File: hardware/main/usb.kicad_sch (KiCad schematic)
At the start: 0 parts

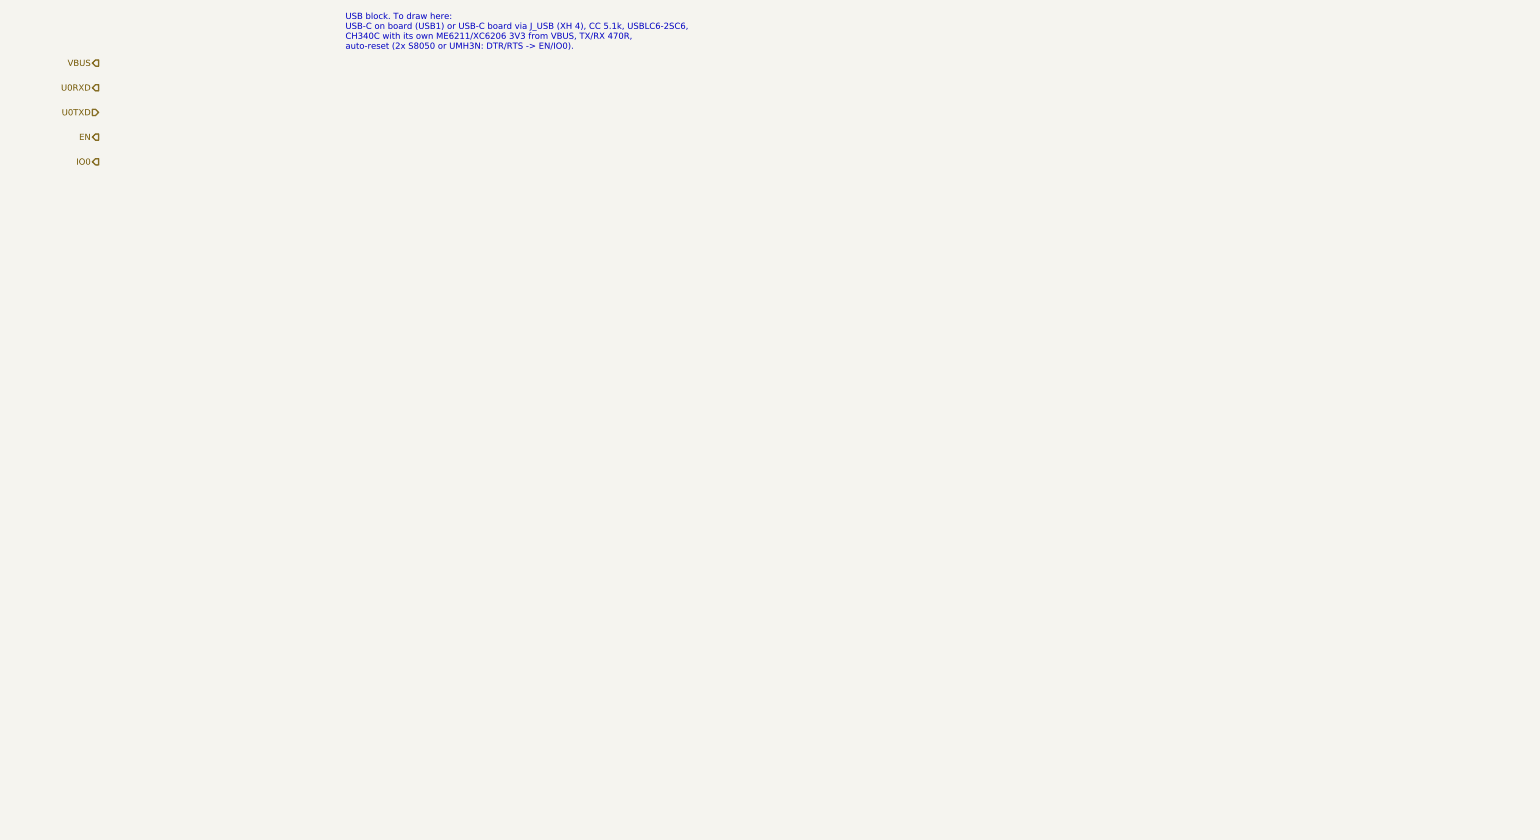
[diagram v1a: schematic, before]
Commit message: hardware: USB, Audio and Connectors sheets; main board ERC clean
Co-Authored-By: Claude Opus 5.5 <noreply@anthropic.com>
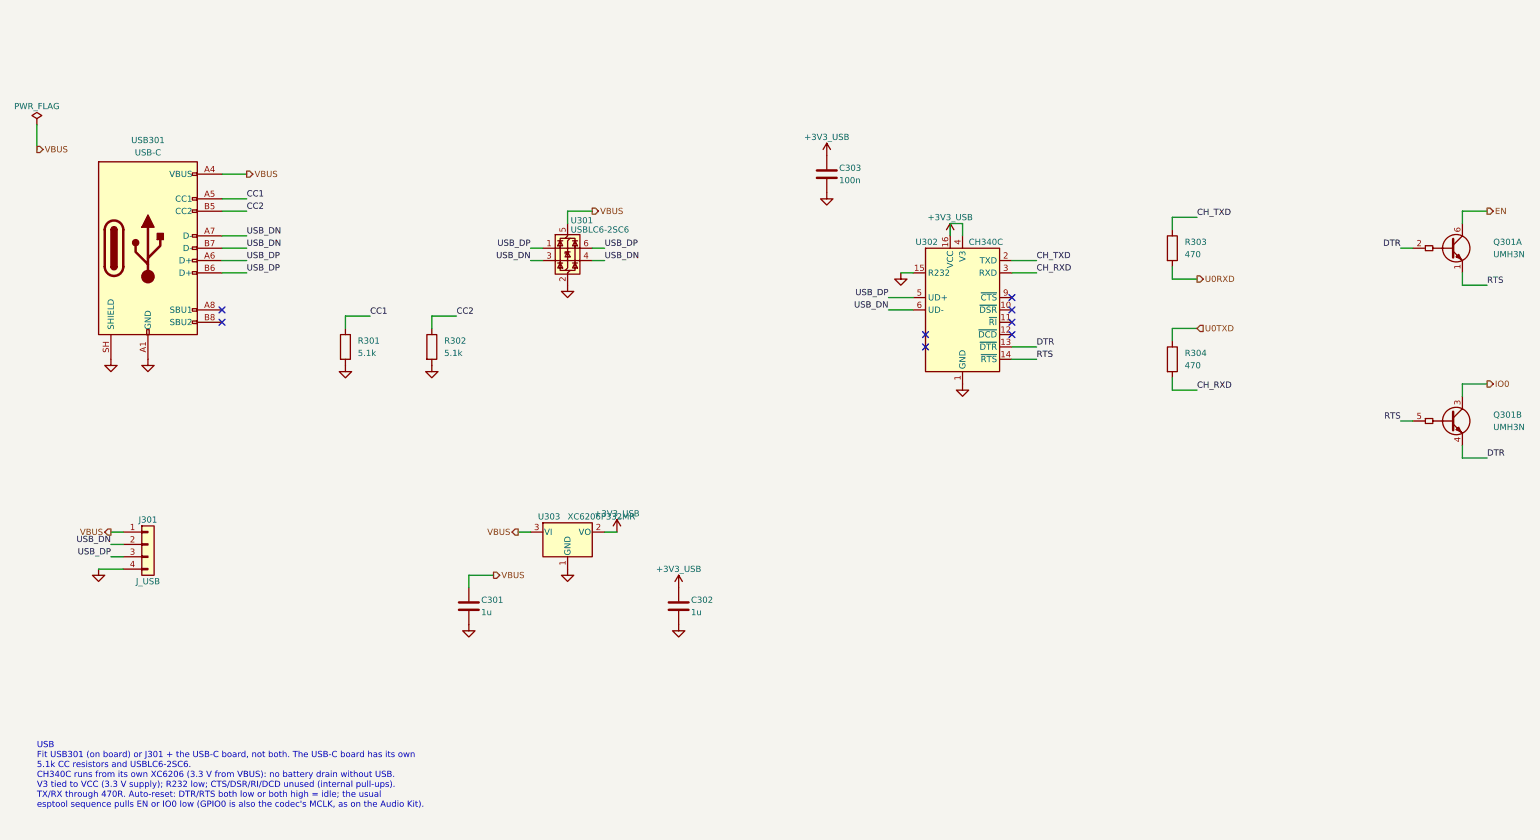
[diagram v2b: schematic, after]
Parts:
- added C301, C302: 1u, Capacitor_SMD:C_0805_2012Metric, symbol Device:C
- added C303: 100n, Capacitor_SMD:C_0805_2012Metric, symbol Device:C
- added J301: J_USB, Connector_JST:JST_XH_B4B-XH-A_1x04_P2.50mm_Vertical, symbol Connector_Generic:Conn_01x04
- added Q301: UMH3N, Package_TO_SOT_SMD:SOT-363_SC-70-6, symbol Transistor_BJT:UMH3N
- added R301, R302: 5.1k, Resistor_SMD:R_0805_2012Metric, symbol Device:R
- added R303, R304: 470, Resistor_SMD:R_0805_2012Metric, symbol Device:R
- added U301: USBLC6-2SC6, Package_TO_SOT_SMD:SOT-23-6, symbol Power_Protection:USBLC6-2SC6
- added U302: CH340C, Package_SO:SOIC-16_3.9x9.9mm_P1.27mm, symbol sendspin-speaker:CH340C
- added U303: XC6206P332MR, Package_TO_SOT_SMD:SOT-23-3, symbol Regulator_Linear:XC6206PxxxMR
- added USB301: USB-C, Connector_USB:USB_C_Receptacle_HRO_TYPE-C-31-M-12, symbol Connector:USB_C_Receptacle_USB2.0_16P
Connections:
- net EN: now also Q301.6 (C1)
- net IO0: now also Q301.3 (C2)
- net U0RXD: now also R303.2
- net U0TXD: now also R304.1
- net VBUS: now also C301.1, J301.1 (Pin_1), U301.5 (VBUS), U303.3 (VI), USB301.A4 (VBUS), USB301.A9 (VBUS), USB301.B4 (VBUS), USB301.B9 (VBUS)
- new net +3V3_USB: C302.1, C303.1, U302.16 (VCC), U302.4 (V3), U303.2 (VO)
- new net CC1: R301.1, USB301.A5 (CC1)
- new net CC2: R302.1, USB301.B5 (CC2)
- new net CH_RXD: R304.2, U302.3 (RXD)
- new net CH_TXD: R303.1, U302.2 (TXD)
- new net DTR: Q301.2 (B1), Q301.4 (E2), U302.13 (~{DTR})
- new net GND: C301.2, C302.2, C303.2, J301.4 (Pin_4), R301.2, R302.2, U301.2 (GND), U302.1 (GND), U302.15 (R232), U303.1 (GND), USB301.A1 (GND), USB301.A12 (GND), USB301.B1 (GND), USB301.B12 (GND), USB301.SH (SHIELD)
- new net RTS: Q301.1 (E1), Q301.5 (B2), U302.14 (~{RTS})
- new net USB_DN: J301.2 (Pin_2), U301.3 (I/O2), U301.4 (I/O2), U302.6 (UD-), USB301.A7 (D-), USB301.B7 (D-)
- new net USB_DP: J301.3 (Pin_3), U301.1 (I/O1), U301.6 (I/O1), U302.5 (UD+), USB301.A6 (D+), USB301.B6 (D+)
- no-connect marks 0 -> 8
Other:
- note added: "USB Fit USB301 (on board) or J301 + the USB-C board, not both. The USB-C board has its own 5.1k CC resistors and USBLC6-2SC6. CH340C runs from its own XC6206 (3.3 V from VBUS): no battery drain without USB. V3 tied to VCC (3.3 V supply); R232 low; CTS/DSR/RI/DCD unused (internal pull-ups). TX/RX through 470R. Auto-reset: DTR/RTS both low or both high = idle; the usual esptool sequence pulls EN or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"
- note removed: "USB block. To draw here: USB-C on board (USB1) or USB-C board via J_USB (XH 4), CC 5.1k, USBLC6-2SC6, CH340C with its own ME6211/XC6206 3V3 from VBUS, TX/RX 470R, auto-reset (2x S8050 or UMH3N: DTR/RTS -> EN/IO0)."

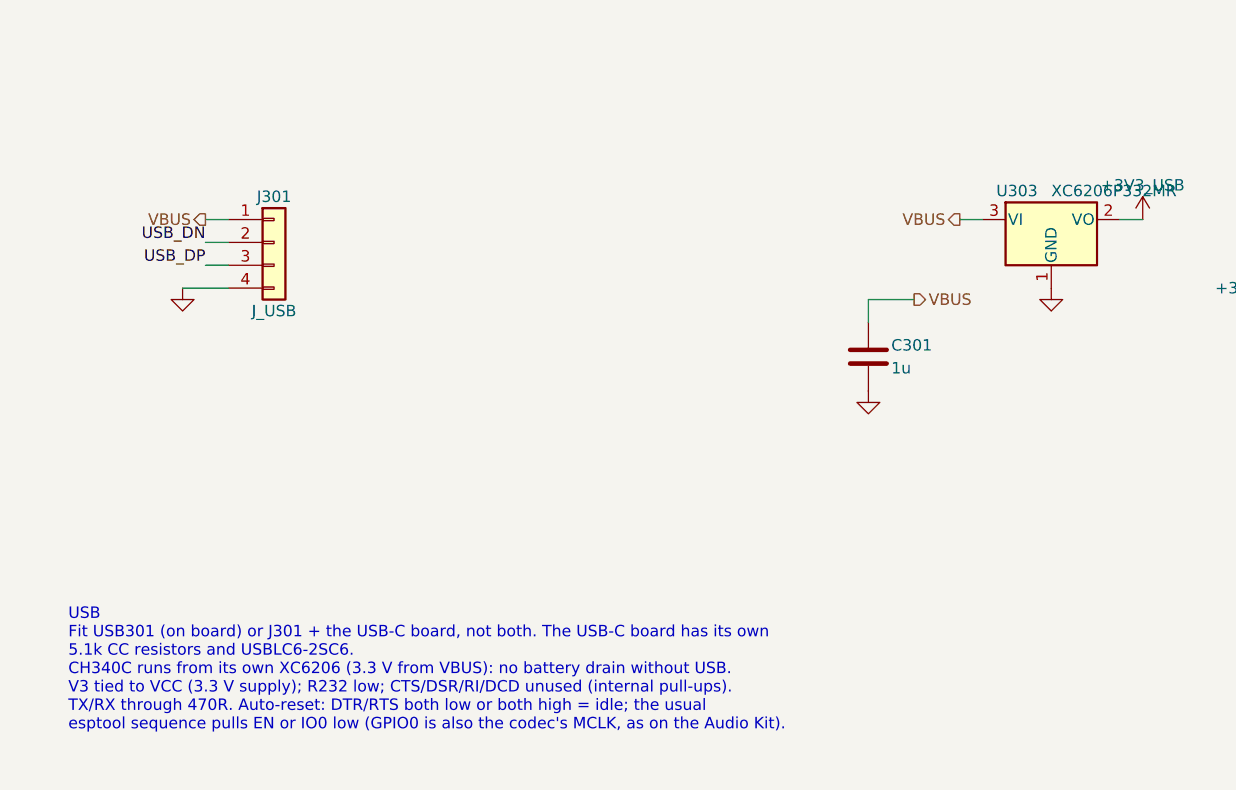
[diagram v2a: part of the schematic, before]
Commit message: hardware: bare USB-C board and front panel (schematics)
J_USB carries CC1/CC2 (XH 6); CC resistors and ESD stay on the main
board. Front panel has only buttons and headers; its LED pin comes
through R501. Boards not yet updated from the schematics.

Co-Authored-By: Claude Opus 5.5 <noreply@anthropic.com>
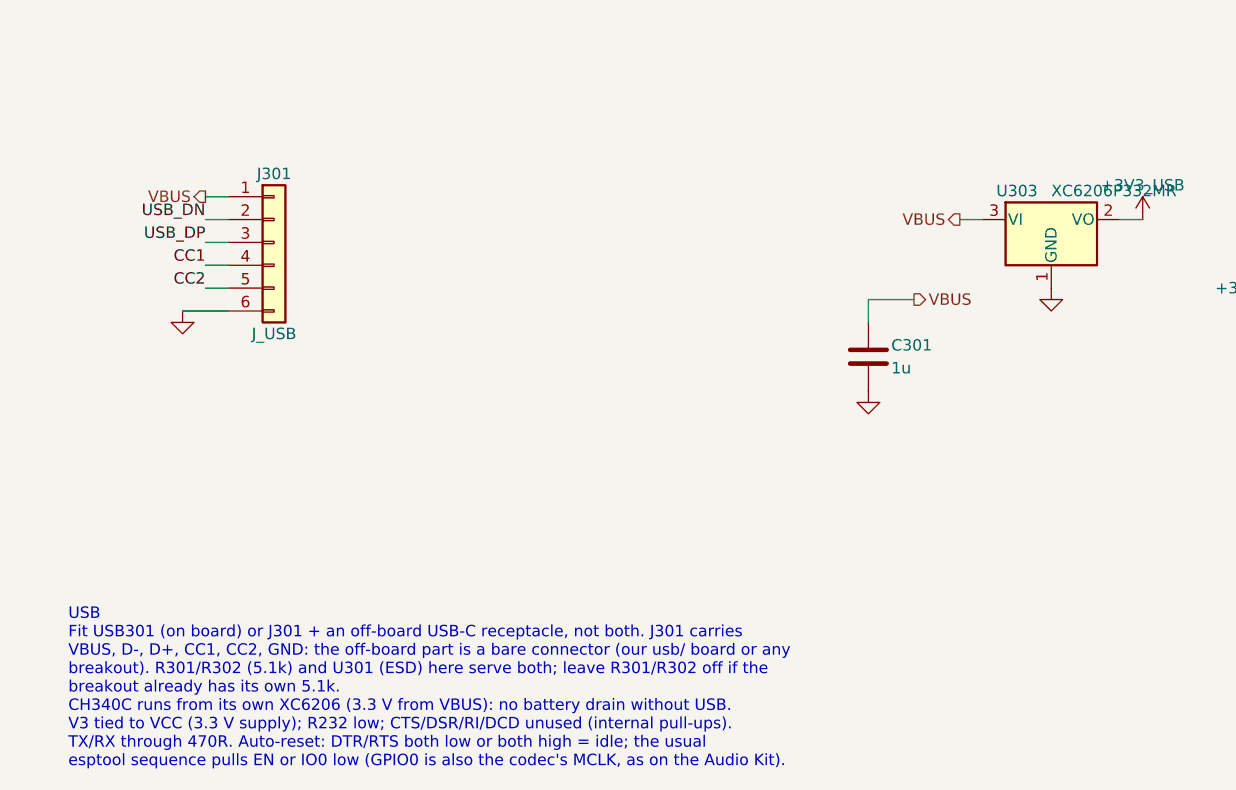
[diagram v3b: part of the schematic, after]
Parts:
- removed J301: J_USB, Connector_JST:JST_XH_B4B-XH-A_1x04_P2.50mm_Vertical, symbol Connector_Generic:Conn_01x04
- added J301: J_USB, Connector_JST:JST_XH_B6B-XH-A_1x06_P2.50mm_Vertical, symbol Connector_Generic:Conn_01x06
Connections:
- net CC1: now also J301.4 (Pin_4)
- net CC2: now also J301.5 (Pin_5)
- net GND: now also J301.6 (Pin_6)
- net USB_DN: now also J301.2 (Pin_2)
- net USB_DP: now also J301.3 (Pin_3)
- net VBUS: now also J301.1 (Pin_1)
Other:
- note added: "USB Fit USB301 (on board) or J301 + an off-board USB-C receptacle, not both. J301 carries VBUS, D-, D+, CC1, CC2, GND: the off-board part is a bare connector (our usb/ board or any breakout). R301/R302 (5.1k) and U301 (ESD) here serve both; leave R301/R302 off if the breakout already has its own 5.1k. CH340C runs from its own XC6206 (3.3 V from VBUS): no battery drain without USB. V3 tied to VCC 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"
- note removed: "USB Fit USB301 (on board) or J301 + the USB-C board, not both. The USB-C board has its own 5.1k CC resistors and USBLC6-2SC6. CH340C runs from its own XC6206 (3.3 V from VBUS): no battery drain without USB. V3 tied to VCC (3.3 V supply); R232 low; CTS/DSR/RI/DCD unused (internal pull-ups). TX/RX through 470R. Auto-reset: DTR/RTS both low or both high = idle; the usual esptool sequence pulls EN or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"

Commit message: hardware: main board routed and labelled, JLC files
- Freerouting (jar, portable Java 25) via scripts/route.py; net classes
  Power 0.8 mm / Supply 0.4 mm so tracks fit the fine-pitch pins.
- Silkscreen pin names and function labels (silk_main.py), references on
  the fab layer, SMD GND pads solid to the pour; board 100 x 58 mm.
- LCSC numbers on all SMD parts (checked on lcsc.com); jlc.py writes the
  Gerber ZIP, BOM and CPL in JLC's formats.

Co-Authored-By: Claude Opus 5.5 <noreply@anthropic.com>
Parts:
- C301, C302: LCSC (none) -> C28323
- C303: LCSC (none) -> C49678
- Q301: LCSC (none) -> C123008
- R301, R302: LCSC (none) -> C27834
- R303, R304: LCSC (none) -> C17710
- U301: LCSC (none) -> C7519
- U302: LCSC (none) -> C84681
- U303: LCSC (none) -> C5446
- USB301: LCSC (none) -> C165948
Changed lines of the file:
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@@
+			)
+		)
+		(property "LCSC" "C84681"
+			(at 0 0 0)
+			(hide yes)
+			(effects
+				(font
+					(size 1.27 1.27)
+				)
 			)
 		)
@@
 			)
 		)
+		(property "LCSC" "C27834"
+			(at 0 0 0)
+			(hide yes)
+			(effects
+				(font
+					(size 1.27 1.27)
+				)
+			)
+		)
 		(property "Description" ""
 			(at 119.38 109.22 0)
@@
 			)
 		)
+		(property "LCSC" "C123008"
+			(at 0 0 0)
+			(hide yes)
+			(effects
+				(font
+					(size 1.27 1.27)
+				)
+			)
+		)
 		(property "Description" ""
 			(at 330.2 88.9 0)
@@
 			)
 		)
+		(property "LCSC" "C5446"
+			(at 0 0 0)
+			(hide yes)
+			(effects
+				(font
+					(size 1.27 1.27)
+				)
+			)
+		)
 		(property "Description" ""
 			(at 147.32 147.32 0)
@@
 			)
 		)
+		(property "LCSC" "C27834"
+			(at 0 0 0)
+			(hide yes)
+			(effects
+				(font
+					(size 1.27 1.27)
+				)
+			)
+		)
 		(property "Description" ""
 			(at 101.6 109.22 0)
@@
 			)
 		)
+		(property "LCSC" "C17710"
+			(at 0 0 0)
+			(hide yes)
+			(effects
+				(font
+					(size 1.27 1.27)
+				)
+			)
+		)
 		(property "Description" ""
 			(at 271.78 88.9 0)
@@
 			)
 		)
+		(property "LCSC" "C28323"
+			(at 0 0 0)
+			(hide yes)
+			(effects
+				(font
+					(size 1.27 1.27)
+				)
+			)
+		)
 		(property "Description" ""
 			(at 127 162.56 0)
@@
 			)
 		)
+		(property "LCSC" "C7519"
+			(at 0 0 0)
+			(hide yes)
+			(effects
+				(font
+					(size 1.27 1.27)
+				)
+			)
+		)
 		(property "Description" ""
 			(at 147.32 88.9 0)
@@
 			)
 		)
+		(property "LCSC" "C28323"
+			(at 0 0 0)
+			(hide yes)
+			(effects
+				(font
+					(size 1.27 1.27)
+				)
+			)
+		)
 		(property "Description" ""
 			(at 170.18 162.56 0)
@@
 			(show_name no)
 			(do_not_autoplace no)
+			(effects
+				(font
+					(size 1.27 1.27)
+				)
+			)
+		)
+		(property "LCSC" "C49678"
+			(at 0 0 0)
+			(hide yes)
 			(effects
 				(font
@@
 			)
 		)
+		(property "LCSC" "C123008"
+			(at 0 0 0)
+			(hide yes)
+			(effects
+				(font
+					(size 1.27 1.27)
+				)
+			)
+		)
 		(property "Description" ""
 			(at 330.2 124.46 0)
@@
 			)
 		)
+		(property "LCSC" "C17710"
+			(at 0 0 0)
+			(hide yes)
+			(effects
+				(font
+					(size 1.27 1.27)
+				)
+			)
+		)
 		(property "Description" ""
 			(at 271.78 111.76 0)
@@
 			(effects
 				(font
+					(size 1.27 1.27)
+				)
+			)
+		)
+		(property "LCSC" "C165948"
+			(at 0 0 0)
+			(hide yes)
+			(effects
+				(font
